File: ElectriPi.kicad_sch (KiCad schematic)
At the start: 55 parts, among them IC2 TPS51397ARJER, J1 2444, J2 JST XH 01x02, J3 JST XH 01x02, J6 Raspberry_Pi_2_3, J8 JST XH 01x02, Q1 SiA471DJ, Q2 SiA430DJT, U1 LM74700, U2 COOLING

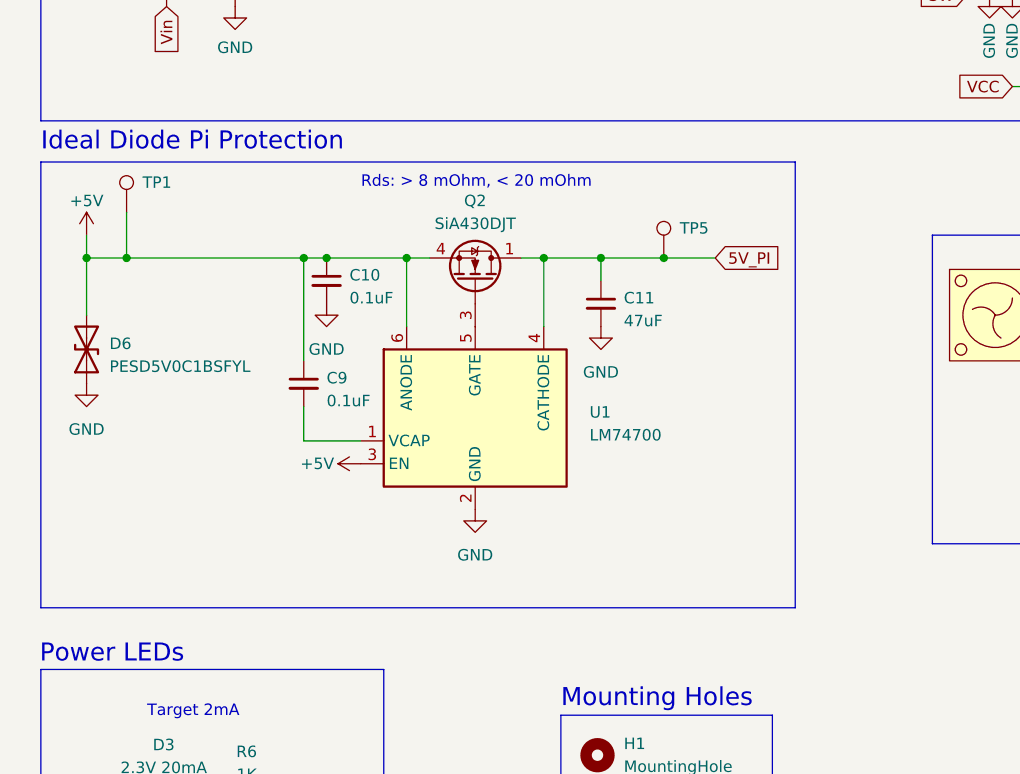
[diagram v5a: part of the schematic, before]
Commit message: Changed back to 0805 35V input caps. With added bulk capacitance derating less of a concern. Cleanup
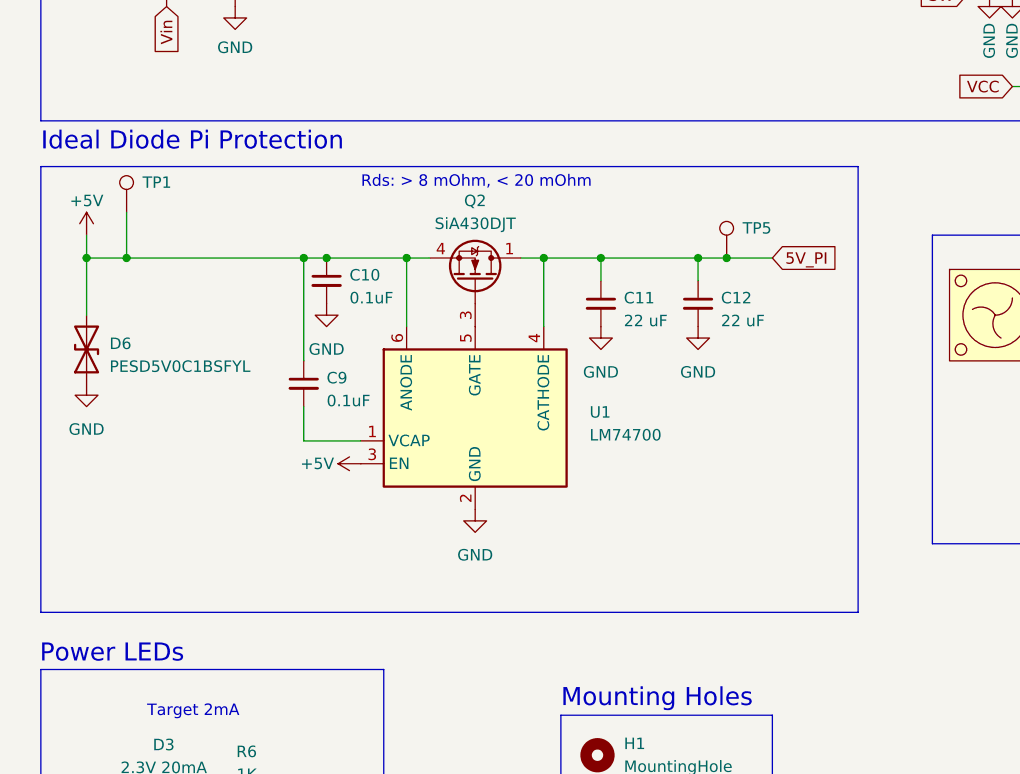
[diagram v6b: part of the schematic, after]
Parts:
- added C12: 22 uF, Capacitor_SMD:C_0805_2012Metric, symbol Device:C_Small
- C1, C2: footprint Capacitor_SMD:C_2220_5650Metric_Pad1.97x5.40mm_HandSolder -> Capacitor_SMD:C_0805_2012Metric; Mouser 810-C5750X7S2A226280 -> 810-C2012X5R1V226MAC
- C11: value 47uF -> 22 uF; Mouser 81-GRM21BR61A476ME5L -> 810-C2012X5R1V226MAC
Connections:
- net 5V_PI: now also C12.1
- net GND: now also C12.2
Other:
- moved on the sheet: TP5
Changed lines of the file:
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@@
   (junction (at 92.075 40.64) (diameter 0) (color 0 0 0 0)
   )
+  (junction (at 93.98 116.84) (diameter 0) (color 0 0 0 0)
+  )
   (junction (at 70.485 40.64) (diameter 0) (color 0 0 0 0)
   )
@@
   (junction (at 49.53 116.84) (diameter 0) (color 0 0 0 0)
   )
-  (junction (at 86.995 116.84) (diameter 0) (color 0 0 0 0)
-  )
   (junction (at 156.21 72.39) (diameter 0) (color 0 0 0 0)
   )
@@
   (junction (at 177.8 50.8) (diameter 0) (color 0 0 0 0)
   )
+  (junction (at 90.805 116.84) (diameter 0) (color 0 0 0 0)
+  )
   (junction (at 73.66 116.84) (diameter 0) (color 0 0 0 0)
   )
@@
     (stroke (width 0) (type default))
   )
+  (wire (pts (xy 93.98 116.84) (xy 99.06 116.84))
+    (stroke (width 0) (type default))
+  )
   (wire (pts (xy 81.915 40.64) (xy 92.075 40.64))
     (stroke (width 0) (type default))
@@
     (stroke (width 0) (type default))
   )
-  (wire (pts (xy 86.995 116.84) (xy 92.71 116.84))
+  (wire (pts (xy 90.805 119.38) (xy 90.805 116.84))
     (stroke (width 0) (type default))
   )
@@
     (stroke (width 0) (type default))
   )
-  (polyline (pts (xy 17.78 106.172) (xy 101.6 106.172))
+  (polyline (pts (xy 17.78 106.68) (xy 108.585 106.68))
     (stroke (width 0) (type default))
   )
@@
     (stroke (width 0) (type default))
   )
+  (wire (pts (xy 90.805 116.84) (xy 93.98 116.84))
+    (stroke (width 0) (type default))
+  )
   (wire (pts (xy 20.32 45.72) (xy 25.4 45.72))
     (stroke (width 0) (type default))
   )
-  (polyline (pts (xy 101.6 155.702) (xy 17.78 155.702))
+  (polyline (pts (xy 108.585 156.21) (xy 17.78 156.21))
     (stroke (width 0) (type default))
   )
@@
     (stroke (width 0) (type default))
   )
-  (wire (pts (xy 80.01 116.84) (xy 86.995 116.84))
+  (wire (pts (xy 80.01 116.84) (xy 90.805 116.84))
     (stroke (width 0) (type default))
   )
@@
     (stroke (width 0) (type default))
   )
-  (polyline (pts (xy 101.6 106.172) (xy 101.6 155.702))
+  (polyline (pts (xy 108.585 106.68) (xy 108.585 156.21))
     (stroke (width 0) (type default))
   )
@@
     (stroke (width 0) (type default))
   )
-  (polyline (pts (xy 17.78 106.172) (xy 17.78 155.702))
+  (polyline (pts (xy 17.78 106.68) (xy 17.78 156.21))
     (stroke (width 0) (type default))
   )
@@
     )
   )
-  (global_label "5V_PI" (shape input) (at 92.71 116.84 0) (fields_autoplaced)
+  (global_label "5V_PI" (shape input) (at 99.06 116.84 0) (fields_autoplaced)
     (effects (font (size 1.27 1.27)) (justify left))
-    (property "Intersheetrefs" "${INTERSHEET_REFS}" (at 100.2636 116.7606 0)
+    (property "Intersheetrefs" "${INTERSHEET_REFS}" (at 106.6136 116.7606 0)
       (effects (font (size 1.27 1.27)) (justify left) hide)
     )
@@
       (effects (font (size 1.27 1.27)) (justify left))
     )
-    (property "Footprint" "Capacitor_SMD:C_2220_5650Metric_Pad1.97x5.40mm_HandSolder" (at 92.075 43.18 0)
+    (property "Footprint" "Capacitor_SMD:C_0805_2012Metric" (at 92.075 43.18 0)
       (effects (font (size 1.27 1.27)) hide)
     )
@@
       (effects (font (size 1.27 1.27)) hide)
     )
-    (property "Mouser" "810-C5750X7S2A226280" (at 92.075 43.18 0)
+    (property "Mouser" "810-C2012X5R1V226MAC" (at 92.075 43.18 0)
       (effects (font (size 1.27 1.27)) hide)
     )
@@
     )
   )
-  (symbol (lib_id "Device:C_Small") (at 80.01 121.92 0) (unit 1)
-    (in_bom yes) (on_board yes) (dnp no) (fields_autoplaced)
-    (property "Reference" "C11" (at 82.55 121.2913 0)
-      (effects (font (size 1.27 1.27)) (justify left))
-    )
-    (property "Value" "47uF" (at 82.55 123.8313 0)
-      (effects (font (size 1.27 1.27)) (justify left))
-    )
-    (property "Footprint" "Capacitor_SMD:C_0805_2012Metric" (at 80.01 121.92 0)
-      (effects (font (size 1.27 1.27)) hide)
-    )
-    (property "Datasheet" "~" (at 80.01 121.92 0)
-      (effects (font (size 1.27 1.27)) hide)
-    )
-    (property "Mouser" "81-GRM21BR61A476ME5L" (at 80.01 121.92 0)
-      (effects (font (size 1.27 1.27)) hide)
-    )
-    (pin "1")
-    (pin "2")
-    (instances
-      (project "ElectriPi"
-        (path "/e63e39d7-6ac0-4ffd-8aa3-1841a4541b55"
-          (reference "C11") (unit 1)
-        )
-      )
-    )
-  )
   (symbol (lib_id "Connector:Screw_Terminal_01x02") (at 27.94 54.61 270) (unit 1)
     (in_bom no) (on_board yes) (dnp no)
@@
     )
   )
-  (symbol (lib_id "Connector:TestPoint") (at 86.995 116.84 0) (unit 1)
+  (symbol (lib_id "Connector:TestPoint") (at 93.98 116.84 0) (unit 1)
     (in_bom yes) (on_board yes) (dnp no) (fields_autoplaced)
-    (property "Reference" "TP5" (at 88.773 113.5379 0)
+    (property "Reference" "TP5" (at 95.758 113.5379 0)
       (effects (font (size 1.27 1.27)) (justify left))
     )
-    (property "Value" "TestPoint" (at 89.535 114.8079 0)
+    (property "Value" "TestPoint" (at 96.52 114.8079 0)
       (effects (font (size 1.27 1.27)) (justify left) hide)
     )
-    (property "Footprint" "TestPoint:TestPoint_Pad_D1.5mm" (at 92.075 116.84 0)
+    (property "Footprint" "TestPoint:TestPoint_Pad_D1.5mm" (at 99.06 116.84 0)
       (effects (font (size 1.27 1.27)) hide)
     )
-    (property "Datasheet" "~" (at 92.075 116.84 0)
+    (property "Datasheet" "~" (at 99.06 116.84 0)
       (effects (font (size 1.27 1.27)) hide)
     )
@@
     )
   )
+  (symbol (lib_id "power:GND") (at 90.805 124.46 0) (unit 1)
+    (in_bom yes) (on_board yes) (dnp no) (fields_autoplaced)
+    (property "Reference" "#PWR038" (at 90.805 130.81 0)
+      (effects (font (size 1.27 1.27)) hide)
+    )
+    (property "Value" "GND" (at 90.805 129.54 0)
+      (effects (font (size 1.27 1.27)))
+    )
+    (property "Footprint" "" (at 90.805 124.46 0)
+      (effects (font (size 1.27 1.27)) hide)
+    )
+    (property "Datasheet" "" (at 90.805 124.46 0)
+      (effects (font (size 1.27 1.27)) hide)
+    )
+    (pin "1")
+    (instances
+      (project "ElectriPi"
+        (path "/e63e39d7-6ac0-4ffd-8aa3-1841a4541b55"
+          (reference "#PWR038") (unit 1)
+        )
+      )
+    )
+  )
   (symbol (lib_id "Device:R_Small") (at 217.17 63.5 0) (unit 1)
     (in_bom yes) (on_board yes) (dnp no) (fields_autoplaced)
@@
     )
   )
+  (symbol (lib_id "Device:C_Small") (at 80.01 121.92 0) (unit 1)
+    (in_bom yes) (on_board yes) (dnp no) (fields_autoplaced)
+    (property "Reference" "C11" (at 82.55 121.2913 0)
+      (effects (font (size 1.27 1.27)) (justify left))
+    )
+    (property "Value" "22 uF" (at 82.55 123.8313 0)
+      (effects (font (size 1.27 1.27)) (justify left))
+    )
+    (property "Footprint" "Capacitor_SMD:C_0805_2012Metric" (at 80.01 121.92 0)
+      (effects (font (size 1.27 1.27)) hide)
+    )
+    (property "Datasheet" "~" (at 80.01 121.92 0)
+      (effects (font (size 1.27 1.27)) hide)
+    )
+    (property "Mouser" "810-C2012X5R1V226MAC" (at 80.01 121.92 0)
+      (effects (font (size 1.27 1.27)) hide)
+    )
+    (pin "1")
+    (pin "2")
+    (instances
+      (project "ElectriPi"
+        (path "/e63e39d7-6ac0-4ffd-8aa3-1841a4541b55"
+          (reference "C11") (unit 1)
+        )
+      )
+    )
+  )
   (symbol (lib_id "power:GND") (at 168.91 62.23 0) (unit 1)
     (in_bom yes) (on_board yes) (dnp no) (fields_autoplaced)
@@
     )
   )
+  (symbol (lib_id "Device:C_Small") (at 90.805 121.92 0) (unit 1)
+    (in_bom yes) (on_board yes) (dnp no) (fields_autoplaced)
+    (property "Reference" "C12" (at 93.345 121.2913 0)
+      (effects (font (size 1.27 1.27)) (justify left))
+    )
+    (property "Value" "22 uF" (at 93.345 123.8313 0)
+      (effects (font (size 1.27 1.27)) (justify left))
+    )
+    (property "Footprint" "Capacitor_SMD:C_0805_2012Metric" (at 90.805 121.92 0)
+      (effects (font (size 1.27 1.27)) hide)
+    )
+    (property "Datasheet" "~" (at 90.805 121.92 0)
+      (effects (font (size 1.27 1.27)) hide)
+    )
+    (property "Mouser" "810-C2012X5R1V226MAC" (at 90.805 121.92 0)
+      (effects (font (size 1.27 1.27)) hide)
+    )
+    (pin "1")
+    (pin "2")
+    (instances
+      (project "ElectriPi"
+        (path "/e63e39d7-6ac0-4ffd-8aa3-1841a4541b55"
+          (reference "C12") (unit 1)
+        )
+      )
+    )
+  )
   (symbol (lib_id "Device:D_TVS") (at 22.86 127 90) (unit 1)
     (in_bom yes) (on_board yes) (dnp no) (fields_autoplaced)
@@
       (effects (font (size 1.27 1.27)) (justify left))
     )
-    (property "Footprint" "Capacitor_SMD:C_2220_5650Metric_Pad1.97x5.40mm_HandSolder" (at 81.915 43.18 0)
+    (property "Footprint" "Capacitor_SMD:C_0805_2012Metric" (at 81.915 43.18 0)
       (effects (font (size 1.27 1.27)) hide)
     )
@@
       (effects (font (size 1.27 1.27)) hide)
     )
-    (property "Mouser" "810-C5750X7S2A226280" (at 81.915 43.18 0)
+    (property "Mouser" "810-C2012X5R1V226MAC" (at 81.915 43.18 0)
       (effects (font (size 1.27 1.27)) hide)
     )

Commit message: added distributor part numbers for several components
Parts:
- C1, C11, C12, C2: JLC (none) -> C2179409
- C18: JLC (none) -> C2165366
- C4, C5: JLC (none) -> C883598; Mouser (none) -> 81-GRM31CR61A107MA8L
- D1: JLC (none) -> C3712593; Mouser (none) -> 78-XMC7K24CAHM3/H
- D4: JLC (none) -> C87090; Mouser (none) -> 771-BZX84-C13-T/R
- D6: JLC (none) -> C477955; Mouser (none) -> 771-PESD5V0C1BSFYL
- IC2: JLC (none) -> C1518754
- Q1: Mouser (none) -> 78-SIA471DJ-T1-GE3
- Q2: JLC (none) -> C727371; Mouser (none) -> 78-SIA430DJT-T1-GE3
- U1: JLC (none) -> C2941042; Mouser (none) -> 595-LM74700QDBVRQ1
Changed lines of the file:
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@@
       (effects (font (size 1.27 1.27)) (justify left top) hide)
+    )
+    (property "JLC" "C1518754" (at 110.49 59.69 0)
+      (effects (font (size 1.27 1.27)) hide)
     )
     (pin "1")
@@
       (effects (font (size 1.27 1.27)) hide)
     )
+    (property "Mouser" "771-BZX84-C13-T/R" (at 67.31 54.61 90)
+      (effects (font (size 1.27 1.27)) hide)
+    )
+    (property "JLC" "C87090" (at 67.31 54.61 90)
+      (effects (font (size 1.27 1.27)) hide)
+    )
     (pin "1")
     (pin "2")
@@
       (effects (font (size 1.27 1.27)) hide)
     )
+    (property "Mouser" "81-GRM31CR61A107MA8L" (at 196.85 55.88 0)
+      (effects (font (size 1.27 1.27)) hide)
+    )
+    (property "JLC" "C883598" (at 196.85 55.88 0)
+      (effects (font (size 1.27 1.27)) hide)
+    )
     (pin "1")
     (pin "2")
@@
       (effects (font (size 1.27 1.27)) hide)
     )
+    (property "JLC" "C2179409" (at 92.075 43.18 0)
+      (effects (font (size 1.27 1.27)) hide)
+    )
     (pin "1")
     (pin "2")
@@
     )
     (property "Mouser" "80-EEV107M050S9MAA" (at 70.485 43.18 0)
+      (effects (font (size 1.27 1.27)) hide)
+    )
+    (property "JLC" "C2165366" (at 70.485 43.18 0)
       (effects (font (size 1.27 1.27)) hide)
     )
@@
       (effects (font (size 1.27 1.27)) (justify left) hide)
     )
+    (property "Mouser" "78-SIA471DJ-T1-GE3" (at 57.15 43.18 90)
+      (effects (font (size 1.27 1.27)) hide)
+    )
     (pin "1")
     (pin "3")
@@
     )
     (property "Mouser" "810-C2012X5R1V226MAC" (at 80.01 121.92 0)
+      (effects (font (size 1.27 1.27)) hide)
+    )
+    (property "JLC" "C2179409" (at 80.01 121.92 0)
       (effects (font (size 1.27 1.27)) hide)
     )
@@
       (effects (font (size 1.27 1.27)) hide)
     )
+    (property "JLC" "C2179409" (at 90.805 121.92 0)
+      (effects (font (size 1.27 1.27)) hide)
+    )
     (pin "1")
     (pin "2")
@@
       (effects (font (size 1.27 1.27)) hide)
     )
+    (property "Mouser" "771-PESD5V0C1BSFYL" (at 22.86 127 90)
+      (effects (font (size 1.27 1.27)) hide)
+    )
+    (property "JLC" "C477955" (at 22.86 127 90)
+      (effects (font (size 1.27 1.27)) hide)
+    )
     (pin "1")
     (pin "2")
@@
     )
     (property "Datasheet" "~" (at 207.01 55.88 0)
+      (effects (font (size 1.27 1.27)) hide)
+    )
+    (property "Mouser" "81-GRM31CR61A107MA8L" (at 207.01 55.88 0)
+      (effects (font (size 1.27 1.27)) hide)
+    )
+    (property "JLC" "C883598" (at 207.01 55.88 0)
       (effects (font (size 1.27 1.27)) hide)
     )
@@
       (effects (font (size 1.27 1.27)) hide)
     )
+    (property "JLC" "C2179409" (at 81.915 43.18 0)
+      (effects (font (size 1.27 1.27)) hide)
+    )
     (pin "1")
     (pin "2")
@@
       (effects (font (size 1.27 1.27)) hide)
     )
+    (property "Mouser" "78-XMC7K24CAHM3/H" (at 41.91 48.26 90)
+      (effects (font (size 1.27 1.27)) hide)
+    )
+    (property "JLC" "C3712593" (at 41.91 48.26 90)
+      (effects (font (size 1.27 1.27)) hide)
+    )
     (pin "1")
     (pin "2")
@@
       (effects (font (size 1.27 1.27)) (justify left) hide)
     )
+    (property "Mouser" "78-SIA430DJT-T1-GE3" (at 66.04 119.38 90)
+      (effects (font (size 1.27 1.27)) hide)
+    )
+    (property "JLC" "C727371" (at 66.04 119.38 90)
+      (effects (font (size 1.27 1.27)) hide)
+    )
     (pin "1")
     (pin "3")
@@
       (effects (font (size 1.27 1.27)) hide)
     )
+    (property "Mouser" "595-LM74700QDBVRQ1" (at 66.04 134.62 0)
+      (effects (font (size 1.27 1.27)) hide)
+    )
+    (property "JLC" "C2941042" (at 66.04 134.62 0)
+      (effects (font (size 1.27 1.27)) hide)
+    )
